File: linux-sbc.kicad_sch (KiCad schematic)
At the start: 9 parts, among them J101 Molex Mini-fit Jr

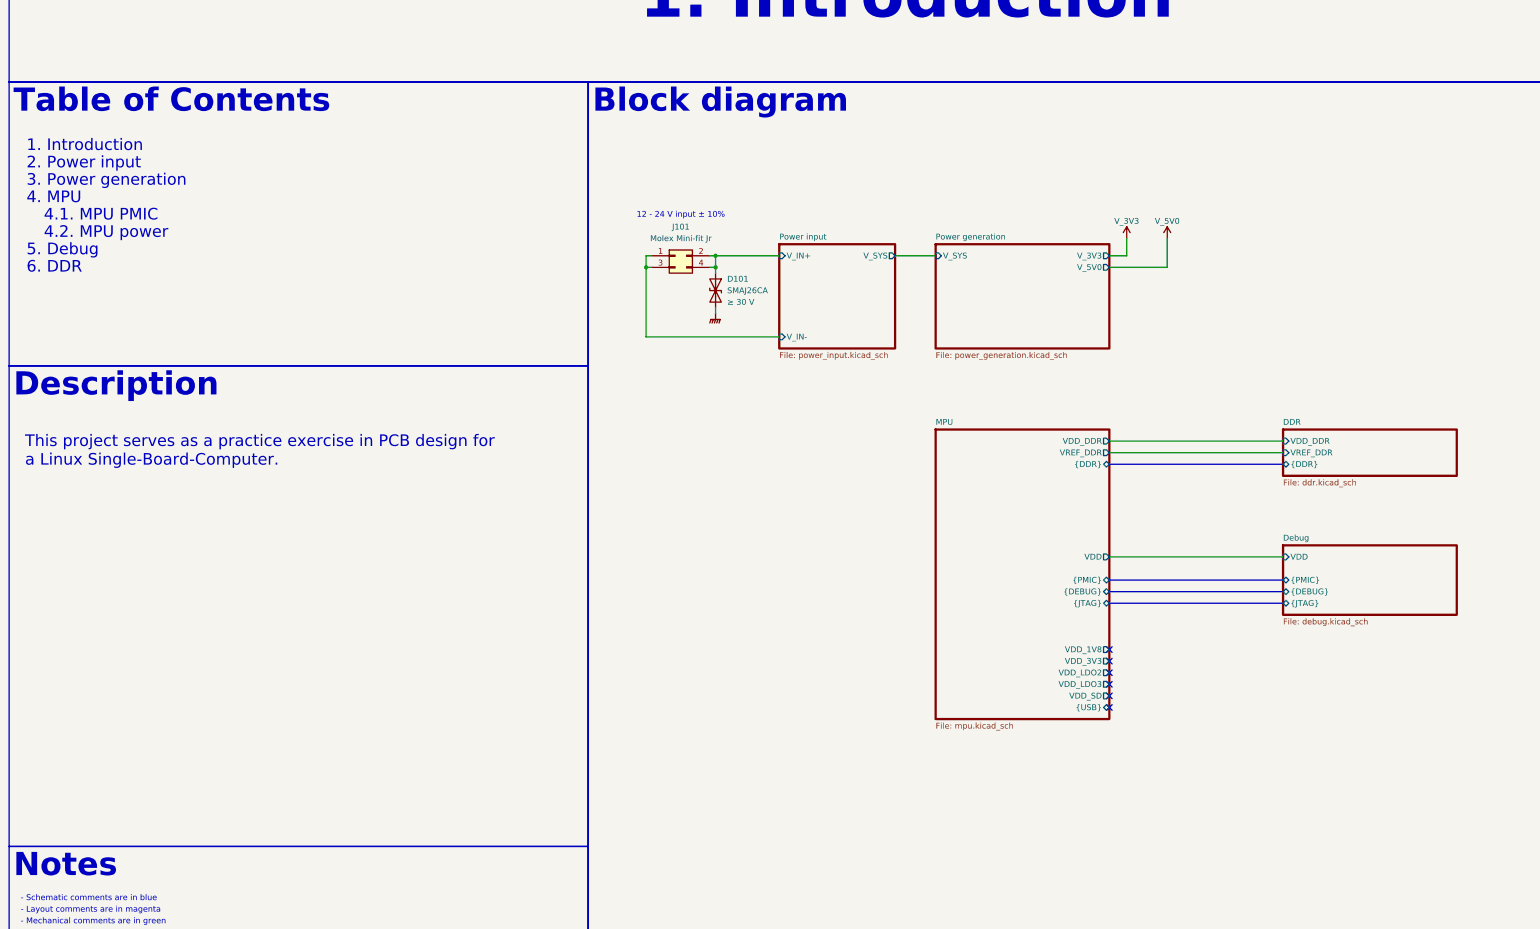
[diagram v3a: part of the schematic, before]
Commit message: Add USB schema
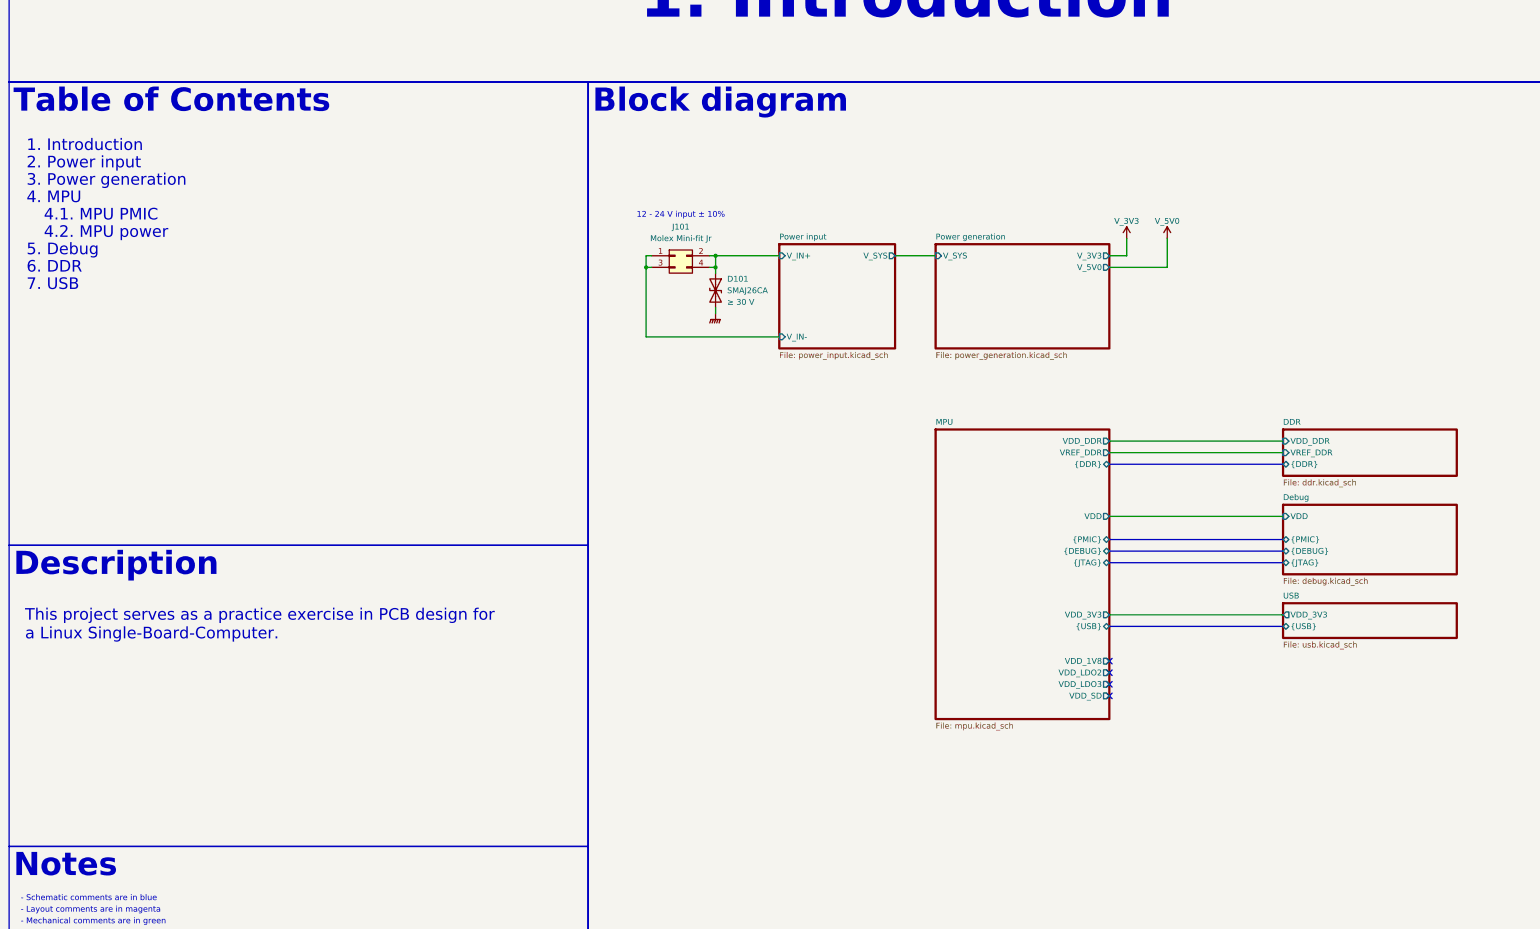
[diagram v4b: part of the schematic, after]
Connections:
- no-connect marks 6 -> 4
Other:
- added sheet USB (usb.kicad_sch)
- note added: "7. USB"
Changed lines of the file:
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@@
 		(rev "v0.0.1")
+	)
+	(text "7. USB"
+		(exclude_from_sim no)
+		(at 16.51 95.25 0)
+		(effects
+			(font
+				(size 2.54 2.54)
+			)
+			(justify left)
+			(href "#9")
+		)
 	)
 	(text "4. MPU"
@@
 		(exclude_from_sim no)
 		(at 12.7 50.8 0)
-		(size 127 62.23)
+		(size 127 101.6)
 		(margins 0.9525 2 0.9525 0.9525)
 		(stroke
@@
 	(text_box "This project serves as a practice exercise in PCB design for a Linux Single-Board-Computer."
 		(exclude_from_sim no)
-		(at 15.24 127 0)
-		(size 123.19 88.9)
+		(at 15.24 165.1 0)
+		(size 123.19 50.8)
 		(margins 0.9525 0.9525 0.9525 0.9525)
 		(stroke
@@
 	(text_box "Description"
 		(exclude_from_sim no)
-		(at 12.7 113.03 0)
-		(size 127 105.41)
+		(at 12.7 152.4 0)
+		(size 127 66.04)
 		(margins 0.9525 2 0.9525 0.9525)
 		(stroke
@@
 	)
 	(no_connect
-		(at 254 175.26)
-	)
-	(no_connect
 		(at 254 177.8)
 	)
@@
 		(at 254 180.34)
 	)
-	(no_connect
-		(at 254 187.96)
-	)
 	(wire
 		(pts
@@
 	(bus
 		(pts
-			(xy 254 162.56) (xy 292.1 162.56)
+			(xy 254 153.67) (xy 292.1 153.67)
 		)
 		(stroke
@@
 	(bus
 		(pts
-			(xy 254 160.02) (xy 292.1 160.02)
+			(xy 254 170.18) (xy 292.1 170.18)
 		)
 		(stroke
@@
 	(bus
 		(pts
+			(xy 254 151.13) (xy 292.1 151.13)
+		)
+		(stroke
+			(width 0)
+			(type default)
+		)
+	)
+	(bus
+		(pts
 			(xy 254 134.62) (xy 292.1 134.62)
 		)
@@
 	(wire
 		(pts
+			(xy 254 167.64) (xy 292.1 167.64)
+		)
+		(stroke
+			(width 0)
+			(type default)
+		)
+	)
+	(wire
+		(pts
 			(xy 167.64 100.33) (xy 167.64 101.6)
 		)
@@
 	(bus
 		(pts
-			(xy 254 165.1) (xy 292.1 165.1)
+			(xy 254 156.21) (xy 292.1 156.21)
 		)
 		(stroke
@@
 	(wire
 		(pts
-			(xy 254 154.94) (xy 292.1 154.94)
+			(xy 254 146.05) (xy 292.1 146.05)
 		)
 		(stroke
@@
 		)
 		(pin "{JTAG}" bidirectional
-			(at 254 165.1 0)
+			(at 254 156.21 0)
 			(effects
 				(font
@@
 		)
 		(pin "{USB}" bidirectional
-			(at 254 187.96 0)
+			(at 254 170.18 0)
 			(effects
 				(font
@@
 		)
 		(pin "VDD_1V8" output
-			(at 254 175.26 0)
+			(at 254 177.8 0)
 			(effects
 				(font
@@
 		)
 		(pin "VDD_3V3" output
-			(at 254 177.8 0)
+			(at 254 167.64 0)
 			(effects
 				(font
@@
 		)
 		(pin "{PMIC}" bidirectional
-			(at 254 160.02 0)
+			(at 254 151.13 0)
 			(effects
 				(font
@@
 		)
 		(pin "{DEBUG}" bidirectional
-			(at 254 162.56 0)
+			(at 254 153.67 0)
 			(effects
 				(font
@@
 		)
 		(pin "VDD" output
-			(at 254 154.94 0)
+			(at 254 146.05 0)
 			(effects
 				(font
@@
 	)
 	(sheet
-		(at 292.1 152.4)
+		(at 292.1 143.51)
 		(size 38.1 15.24)
 		(exclude_from_sim no)
@@
 		)
 		(property "Sheetname" "Debug"
-			(at 292.1 151.5146 0)
+			(at 292.1 142.6246 0)
 			(effects
 				(font
@@
 		)
 		(property "Sheetfile" "debug.kicad_sch"
-			(at 292.1 168.3984 0)
+			(at 292.1 159.5084 0)
 			(effects
 				(font
@@
 		)
 		(pin "{DEBUG}" bidirectional
-			(at 292.1 162.56 180)
+			(at 292.1 153.67 180)
 			(effects
 				(font
@@
 		)
 		(pin "VDD" input
-			(at 292.1 154.94 180)
+			(at 292.1 146.05 180)
 			(effects
 				(font
@@
 		)
 		(pin "{JTAG}" bidirectional
-			(at 292.1 165.1 180)
+			(at 292.1 156.21 180)
 			(effects
 				(font
@@
 		)
 		(pin "{PMIC}" bidirectional
-			(at 292.1 160.02 180)
+			(at 292.1 151.13 180)
 			(effects
 				(font
@@
 				)
 			)
+		)
+	)
+	(sheet
+		(at 292.1 165.1)
+		(size 38.1 7.62)
+		(exclude_from_sim no)
+		(in_bom yes)
+		(on_board yes)
+		(dnp no)
+		(fields_autoplaced yes)
+		(stroke
+			(width 0.5)
+			(type solid)
+			(color 255 255 0 1)
+		)
+		(fill
+			(color 0 255 0 1.0000)
+		)
+		(property "Sheetname" "USB"
+			(at 292.1 164.2146 0)
+			(effects
+				(font
+					(size 1.27 1.27)
+				)
+				(justify left bottom)
+			)
+		)
+		(property "Sheetfile" "usb.kicad_sch"
+			(at 292.1 173.4784 0)
+			(effects
+				(font
+					(size 1.27 1.27)
+				)
+				(justify left top)
+			)
+		)
+		(pin "{USB}" bidirectional
+			(at 292.1 170.18 180)
+			(effects
+				(font
+					(size 1.27 1.27)
+				)
+				(justify left)
+			)
+		)
+		(pin "VDD_3V3" output
+			(at 292.1 167.64 180)
+			(effects
+				(font
+					(size 1.27 1.27)
+				)
+				(justify left)
+			)
+		)
+		(instances
+			(project "linux-sbc"
+				(path "/fa11a02f-8043-4153-ab69-88d766503017"
+					(page "9")
+				)
+			)

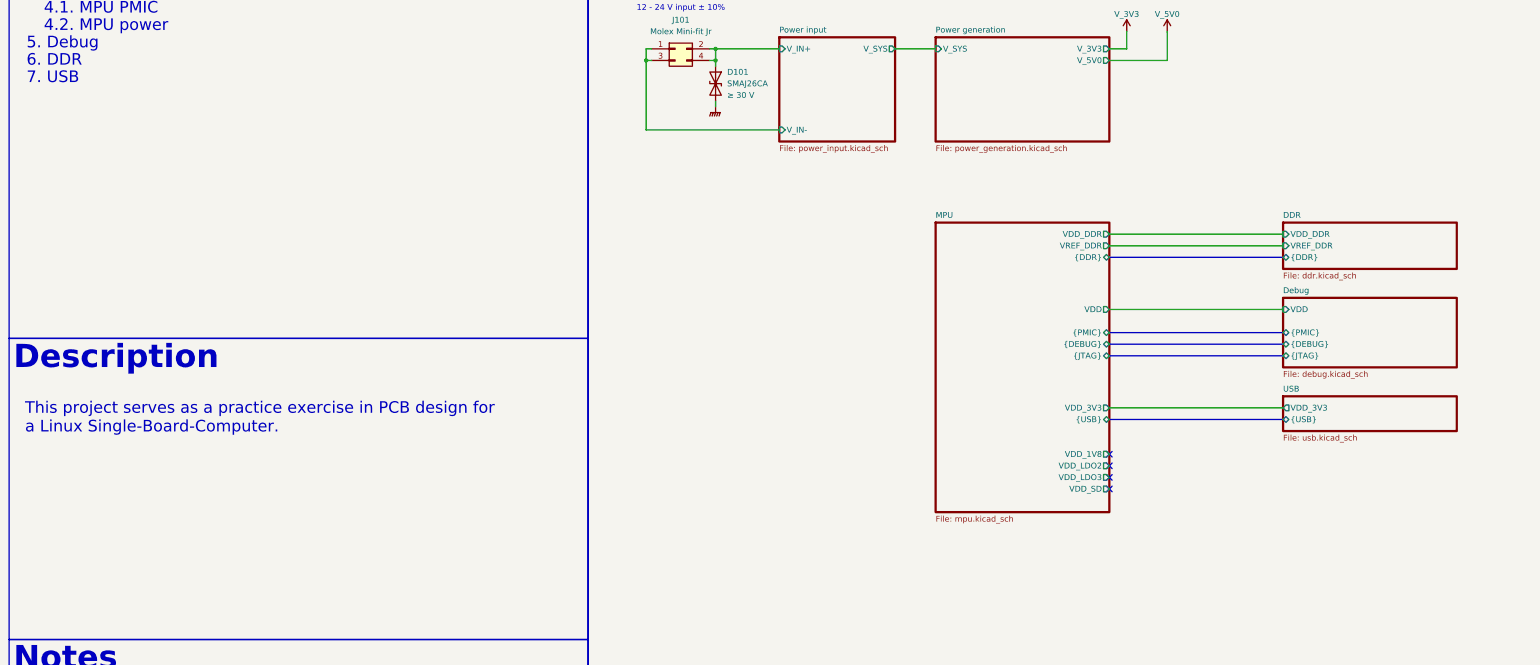
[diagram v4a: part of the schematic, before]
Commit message: Add ETH schema
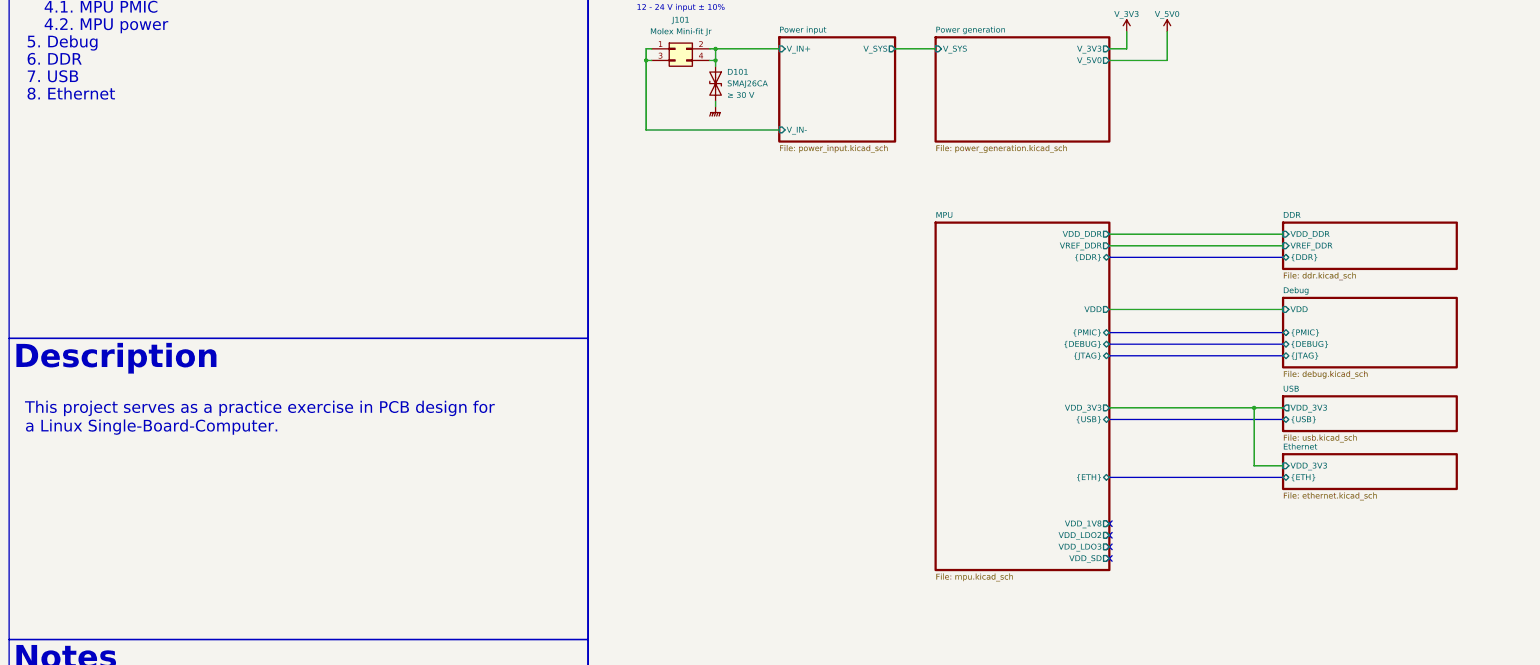
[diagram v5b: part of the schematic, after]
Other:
- added sheet Ethernet (ethernet.kicad_sch)
- sheet MPU ports: added {ETH}; removed none
- note added: "8. Ethernet"
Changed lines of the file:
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@@
+		)
+	)
+	(text "8. Ethernet"
+		(exclude_from_sim no)
+		(at 16.51 99.06 0)
+		(effects
+			(font
+				(size 2.54 2.54)
+			)
+			(justify left)
+			(href "#10")
 		)
 	)
@@
 	)
 	(junction
+		(at 285.75 167.64)
+		(diameter 0)
+		(color 0 0 0 0)
+	)
+	(junction
 		(at 167.64 88.9)
 		(diameter 0)
@@
 	)
 	(no_connect
-		(at 254 182.88)
+		(at 254 198.12)
 	)
 	(no_connect
-		(at 254 185.42)
+		(at 254 200.66)
 	)
 	(no_connect
-		(at 254 177.8)
+		(at 254 193.04)
 	)
 	(no_connect
-		(at 254 180.34)
+		(at 254 195.58)
 	)
 	(wire
@@
 	(wire
 		(pts
+			(xy 285.75 167.64) (xy 292.1 167.64)
+		)
+		(stroke
+			(width 0)
+			(type default)
+		)
+	)
+	(wire
+		(pts
 			(xy 166.37 91.44) (xy 167.64 91.44)
 		)
@@
 		)
 	)
+	(bus
+		(pts
+			(xy 254 182.88) (xy 292.1 182.88)
+		)
+		(stroke
+			(width 0)
+			(type default)
+		)
+	)
+	(wire
+		(pts
+			(xy 285.75 180.34) (xy 292.1 180.34)
+		)
+		(stroke
+			(width 0)
+			(type default)
+		)
+	)
 	(wire
 		(pts
@@
 	(wire
 		(pts
-			(xy 254 167.64) (xy 292.1 167.64)
+			(xy 254 167.64) (xy 285.75 167.64)
 		)
 		(stroke
@@
 		(pts
 			(xy 57.15 278.13) (xy 57.15 279.4)
+		)
+		(stroke
+			(width 0)
+			(type default)
+		)
+	)
+	(wire
+		(pts
+			(xy 285.75 167.64) (xy 285.75 180.34)
 		)
 		(stroke
@@
 	(sheet
 		(at 215.9 127)
-		(size 38.1 63.5)
+		(size 38.1 76.2)
 		(exclude_from_sim no)
 		(in_bom yes)
@@
 		)
 		(property "Sheetfile" "mpu.kicad_sch"
-			(at 215.9 191.2584 0)
+			(at 215.9 203.9584 0)
 			(effects
 				(font
@@
 		)
 		(pin "VDD_1V8" output
-			(at 254 177.8 0)
+			(at 254 193.04 0)
 			(effects
 				(font
@@
 		)
 		(pin "VDD_LDO2" output
-			(at 254 180.34 0)
+			(at 254 195.58 0)
 			(effects
 				(font
@@
 		)
 		(pin "VDD_LDO3" output
-			(at 254 182.88 0)
+			(at 254 198.12 0)
 			(effects
 				(font
@@
 		)
 		(pin "VDD_SD" output
-			(at 254 185.42 0)
+			(at 254 200.66 0)
 			(effects
 				(font
@@
 		(pin "VDD_DDR" output
 			(at 254 129.54 0)
+			(effects
+				(font
+					(size 1.27 1.27)
+				)
+				(justify right)
+			)
+		)
+		(pin "{ETH}" bidirectional
+			(at 254 182.88 0)
 			(effects
 				(font
@@
 				)
 			)
+		)
+	)
+	(sheet
+		(at 292.1 177.8)
+		(size 38.1 7.62)
+		(exclude_from_sim no)
+		(in_bom yes)
+		(on_board yes)
+		(dnp no)
+		(fields_autoplaced yes)
+		(stroke
+			(width 0.5)
+			(type solid)
+			(color 255 255 0 1)
+		)
+		(fill
+			(color 0 255 0 1.0000)
+		)
+		(property "Sheetname" "Ethernet"
+			(at 292.1 176.9146 0)
+			(effects
+				(font
+					(size 1.27 1.27)
+				)
+				(justify left bottom)
+			)
+		)
+		(property "Sheetfile" "ethernet.kicad_sch"
+			(at 292.1 186.1784 0)
+			(effects
+				(font
+					(size 1.27 1.27)
+				)
+				(justify left top)
+			)
+		)
+		(pin "VDD_3V3" input
+			(at 292.1 180.34 180)
+			(effects
+				(font
+					(size 1.27 1.27)
+				)
+				(justify left)
+			)
+		)
+		(pin "{ETH}" bidirectional
+			(at 292.1 182.88 180)
+			(effects
+				(font
+					(size 1.27 1.27)
+				)
+				(justify left)
+			)
+		)
+		(instances
+			(project "linux-sbc"
+				(path "/fa11a02f-8043-4153-ab69-88d766503017"
+					(page "10")
+				)
+			)
